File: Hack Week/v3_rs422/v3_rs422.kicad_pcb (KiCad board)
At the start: 2 copper layers, 17.5 x 17 mm, 3 parts, among them J1 DE9_Socket, J2 Conn_01x04_Socket, U1 MAX3490xSA

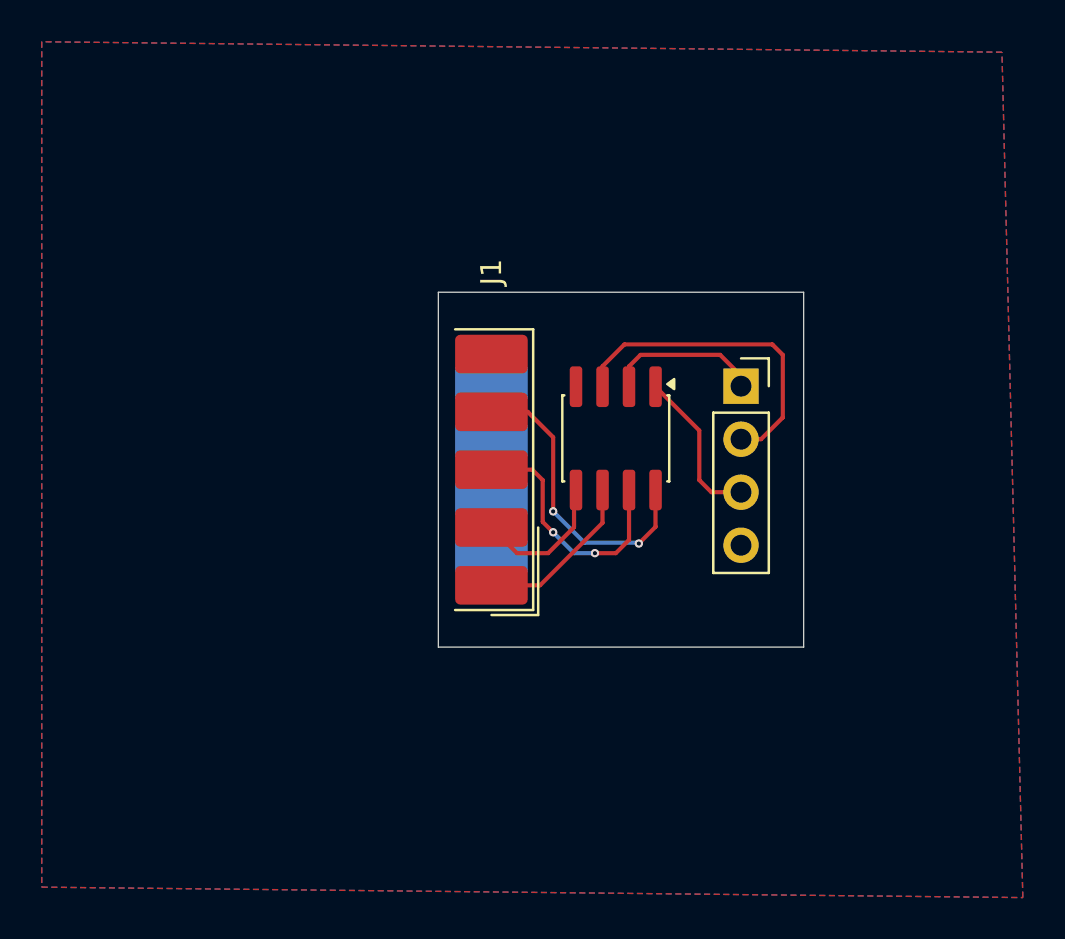
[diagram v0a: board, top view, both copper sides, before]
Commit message: changed DB9 connectors + added RS485
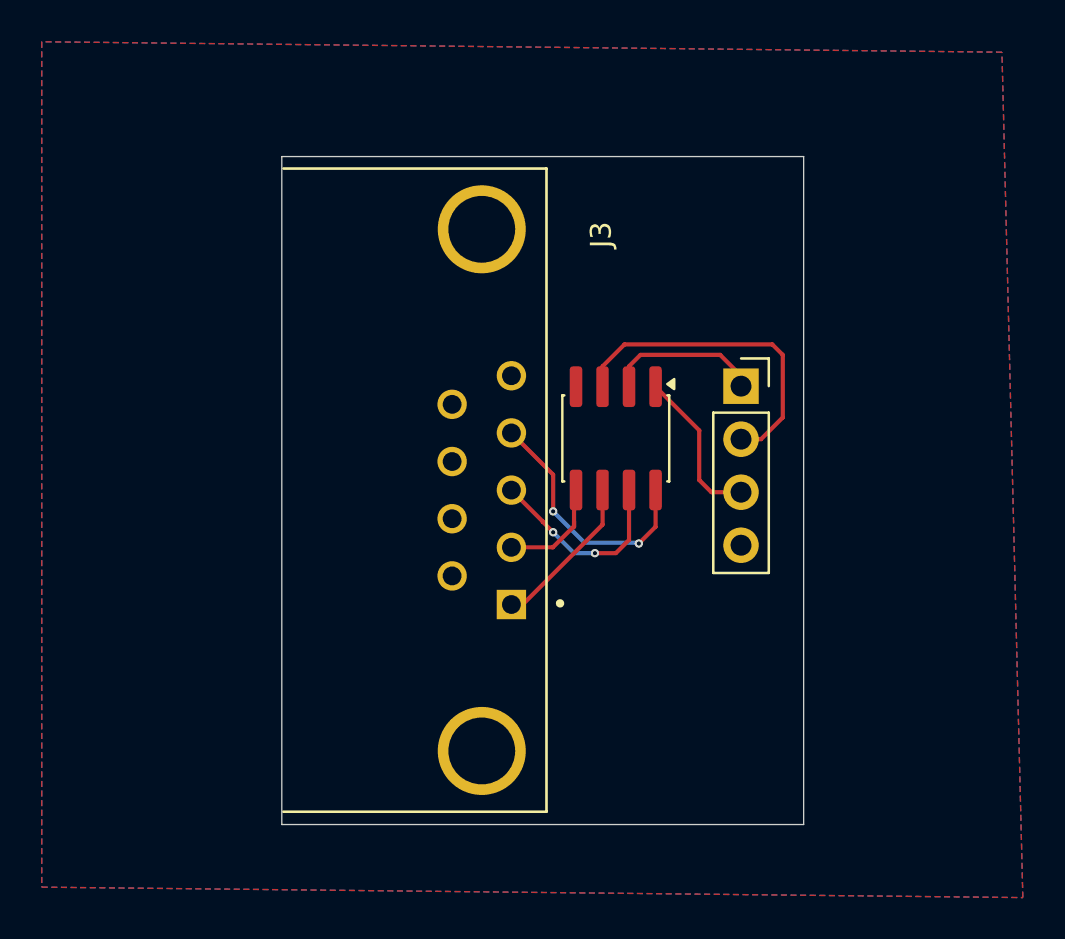
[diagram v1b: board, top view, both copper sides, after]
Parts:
- removed J1: DE9_Socket, Connector_Dsub:DSUB-9_Socket_EdgeMount_P2.77mm
- added J3: LD09S33E4GV00LF, Connector_Pin:AMPHENOL_LD09S33E4GV00LF, F.Cu at (164.1, 63.0)
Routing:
- net /RX+: track 12.1 -> 9.55 mm
- net /RX-: track 14.7 -> 12.2 mm
- net /TX+: track 6.67 -> 5.31 mm
- net /TX-: track 8.13 -> 7.61 mm
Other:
- board size 17.5 x 17 mm -> 25 x 32 mm
